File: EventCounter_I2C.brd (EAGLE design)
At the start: 38.7 x 20.8 mm, 32 parts, among them J1 CONN_42.54_SCREW, J2 CONN_32.54_SCREW, Q3 DMG3404, U1 TLV3691DCK, U11 SN74AUP3G34DCU, U12 TXS0102DQM, U2 TPS7A0533DBV, U7 ATTINY441/841VQFN, U8 SN74AUP1G34SC70

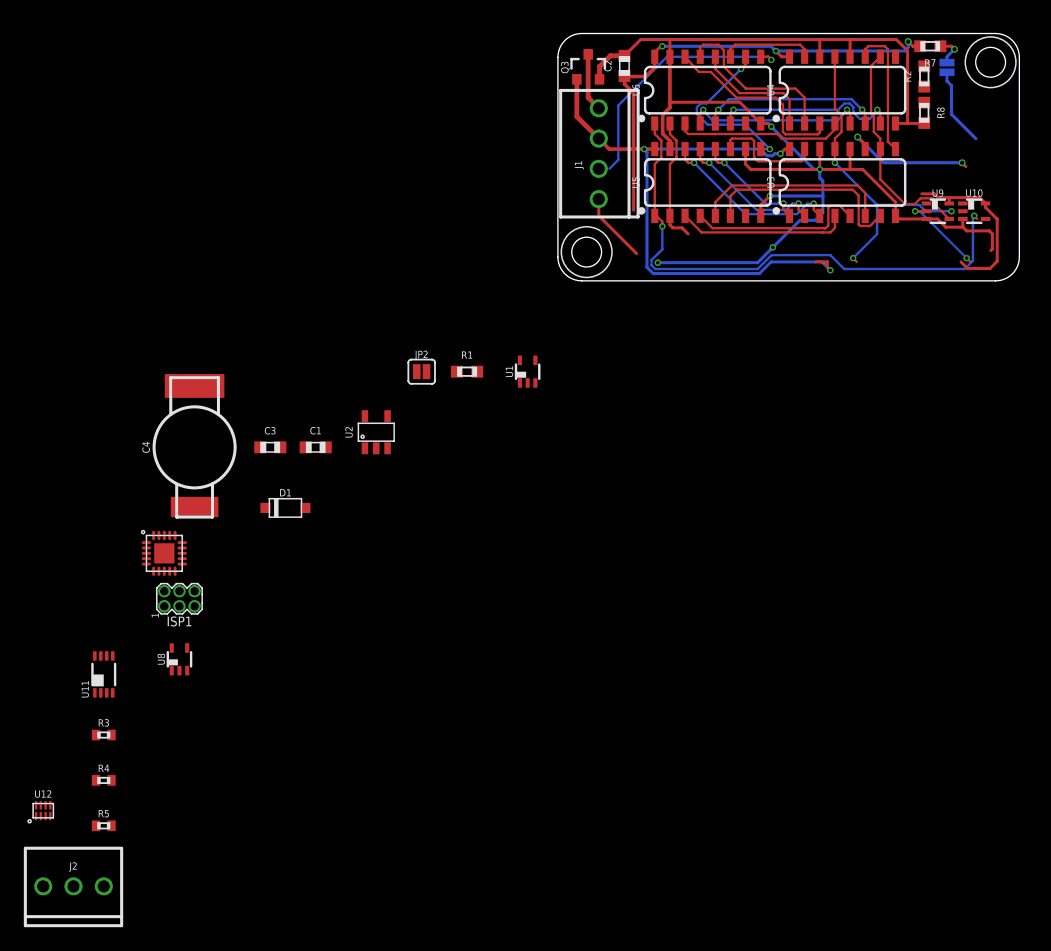
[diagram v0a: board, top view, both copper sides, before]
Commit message: Initial layout for I2C variant
First cut layout for I2C variant, passes DRC, still needs verification
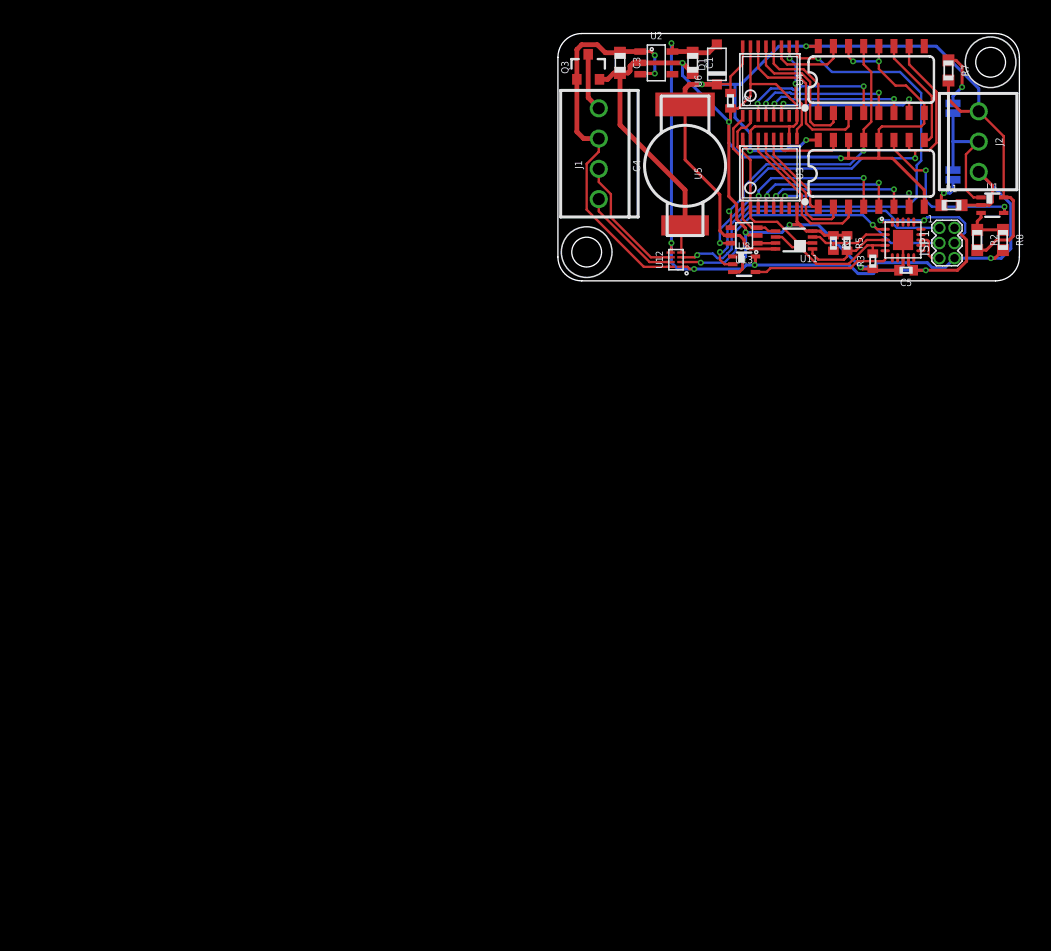
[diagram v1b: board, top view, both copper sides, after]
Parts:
- removed U10, U9: (no value), bschulz:DCK_R-PDSO-G5
- added C5: (no value), bschulz_passives:C0402
- added U13: (no value), bschulz:DCK_R-PDSO-G6
- C2: device bschulz_passives:C0603 -> bschulz_passives:C0402
- U5, U6: device bschulz:SO16 -> bschulz:TSSOP16
- moved J2 98.3 mm to (35.3, 11.7), turned to 270 degrees
- moved R5 79.2 mm to (24.3, 3.17), turned to 270 degrees
- moved R4 76.0 mm to (23.1, 3.17), turned to 270 degrees
- moved R3 75.8 mm to (26.4, 1.65), turned to 90 degrees
- moved ISP1 71.0 mm to (32.6, 3.17), turned to 270 degrees
- moved U12 70.4 mm to (9.91, 1.78), turned to 90 degrees
- moved U11 68.4 mm to (19.8, 3.43), turned to 90 degrees
- moved U7 67.3 mm to (29.0, 3.43)
- moved U8 57.8 mm to (15.6, 1.40), turned to 270 degrees
- moved D1 51.9 mm to (13.3, 18.2), turned to 90 degrees
- moved JP2 47.5 mm to (33.1, 8.89), flipped to the bottom, turned to 270 degrees
- moved C4 47.4 mm to (10.7, 9.65)
- moved C1 45.2 mm to (11.3, 18.3), turned to 270 degrees
- moved C3 43.6 mm to (5.21, 18.3), turned to 270 degrees
- moved R1 43.0 mm to (33.0, 6.35)
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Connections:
- removed net VCC: C2.1, C3.1, J1.3, Q3.1, R2.2, R7.2, U10.5, U12.8, U2.1, U2.3, U3.16, U4.16, U5.16, U6.16, U9.5
- new net VIN+: C3.1, J1.3, Q3.1, U12.8, U2.1, U2.3
- net !LOAD: now also U13.4; no longer U10.4
- net !RST: now also U13.6; no longer U9.4
- net 3V3: now also C5.1
- net CLK: now also U11.2; no longer U11.7
- net CLK_ISO: now also U11.6, U7.4; no longer U11.1
- net DATA_ISO: now also U7.5
- net GND: now also C5.2, U13.2; no longer U10.3, U9.3
- net LOAD: now also U11.5, U13.3; no longer U10.2, U11.2
- net LOAD_ISO: now also U11.3, U7.2; no longer U11.6
- net RST: now also U11.7, U13.1; no longer U11.5, U9.2
- net RST_ISO: now also U11.1, U7.3; no longer U11.3
- net V_CAP: now also C2.1, R2.2, R7.2, U13.5, U3.16, U4.16, U5.16, U6.16
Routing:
- net VCC: track 107.4 -> 0.00 mm, vias 6 -> 0
- net V_CAP: track 0.00 -> 89.4 mm, vias 0 -> 4
- net 3V3: track 0.00 -> 57.2 mm, vias 0 -> 5
- net GND: track 120.9 -> 161.0 mm, vias 5 -> 10
- net VIN+: track 0.00 -> 34.3 mm, vias 0 -> 2
- net LOAD: track 45.7 -> 12.5 mm, vias 2 -> 0
- net SDA: track 0.00 -> 30.3 mm, vias 0 -> 2
- net SCL: track 0.00 -> 26.5 mm, vias 0 -> 2
- net DATA: track 21.3 -> 42.7 mm, vias 1 -> 2
- net !RST: track 18.7 -> 34.6 mm, vias 0 -> 2
- net DATA_ISO: track 0.00 -> 12.0 mm
- net CLK_ISO: track 0.00 -> 11.4 mm
- net SDA_HV: track 0.00 -> 10.9 mm
- net RST_ISO: track 0.00 -> 7.69 mm
- net LOAD_ISO: track 0.00 -> 7.24 mm
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
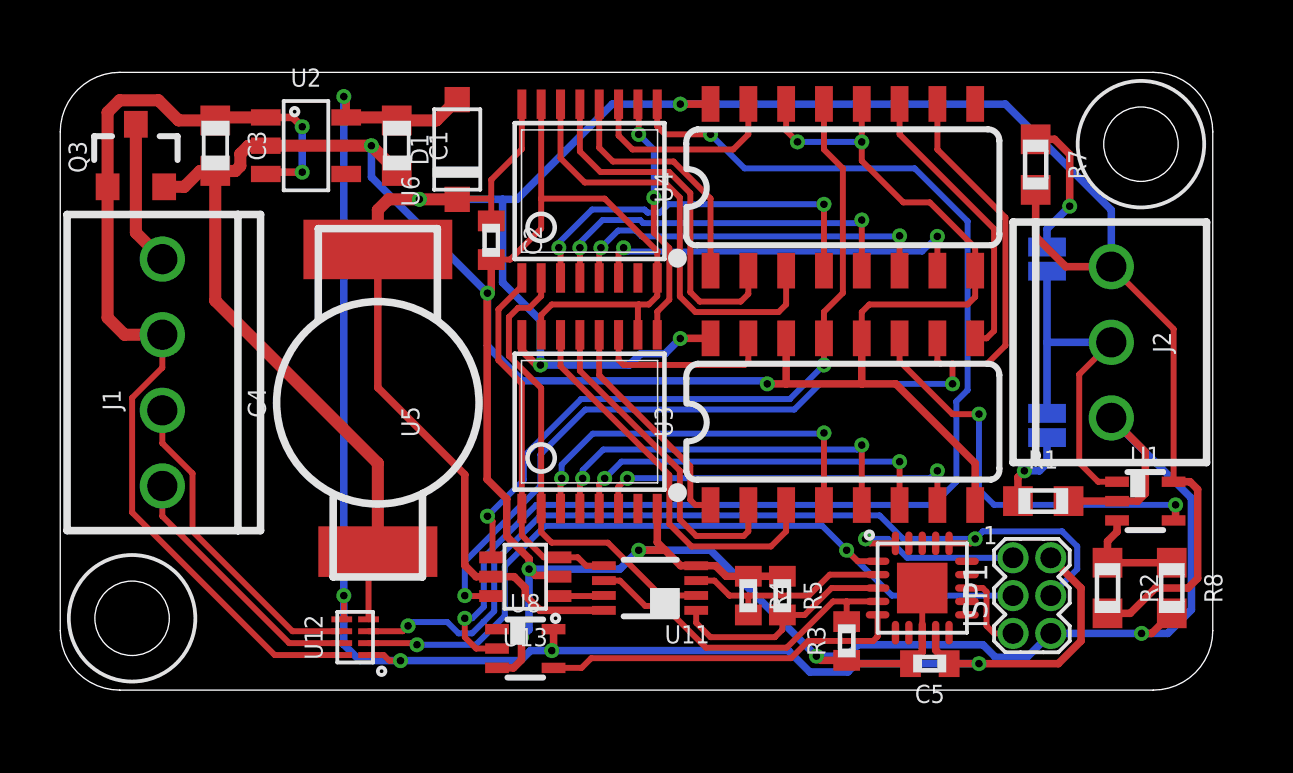
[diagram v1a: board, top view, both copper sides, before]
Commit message: Minor edits, sent to fab for v1.0 (I2C model)
Cleaned up layout, added pullup reset resistor, generated gerbers, sent v1.0 to fab
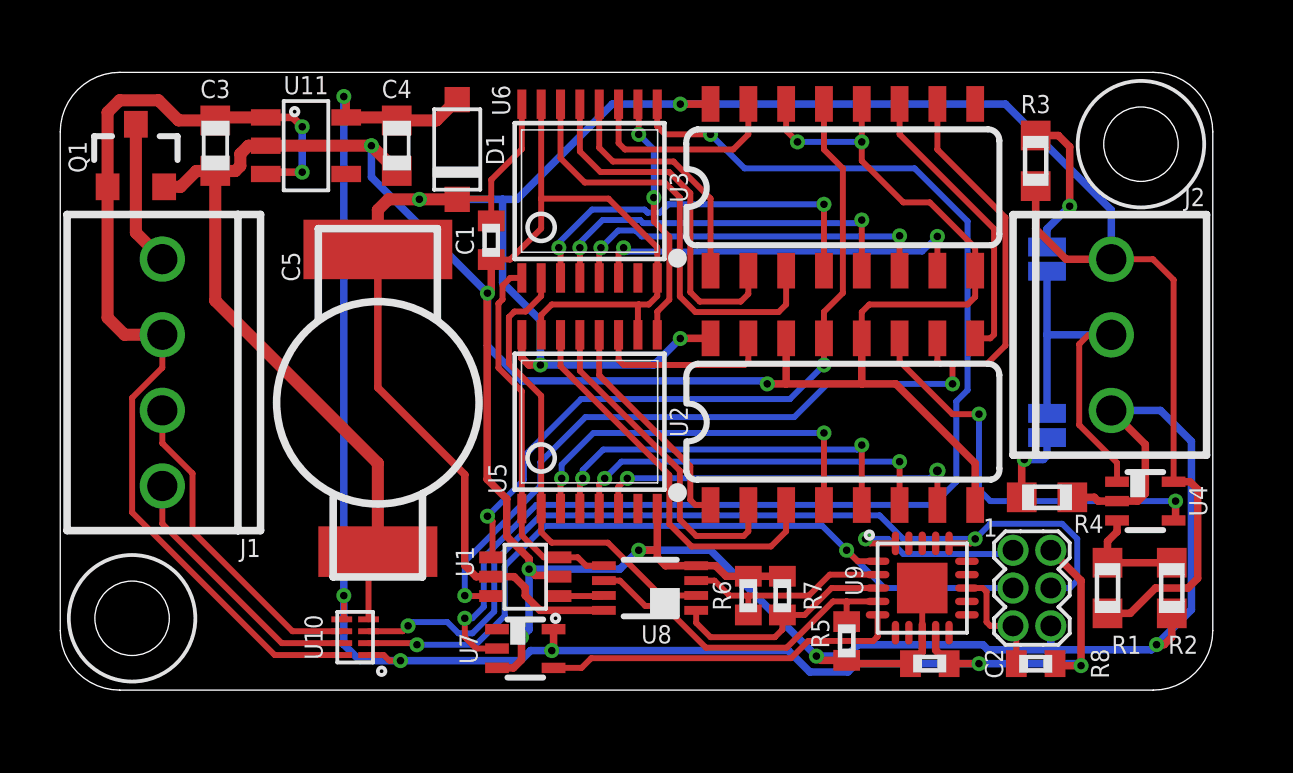
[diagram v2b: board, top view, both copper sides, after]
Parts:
- removed U13: (no value), bschulz:DCK_R-PDSO-G6
- added R6: 10k, bschulz_passives:R0402
- added U9: ATTINY441/841VQFN, bschulz:VQFN-20
- C1: value 1uF -> 0.1uF; device bschulz_passives:C0603 -> bschulz_passives:C0402
- C2: value 0.1uF -> (none)
- C4: value (none) -> 1uF; device bschulz_passives:HL -> bschulz_passives:C0603
- C5: device bschulz_passives:C0402 -> bschulz_passives:HL
- R3: value 10k -> 100k; device bschulz_passives:R0402 -> bschulz_passives:R0603
- R4: value 10k -> 10M; device bschulz_passives:R0402 -> bschulz_passives:R0603
- R7: value 100k -> 10k; device bschulz_passives:R0603 -> bschulz_passives:R0402
- R8: value 10M -> (none); device bschulz_passives:R0603 -> bschulz_passives:R0402
- U1: value TLV3691DCK -> (none); device bschulz:DCK_R-PDSO-G5 -> bschulz:DCK_R-PDSO-G6
- U11: value SN74AUP3G34DCU -> TPS7A0533DBV; device bschulz:DCU_(R-PDSO-G8) -> bschulz:SOT23-5
- U2: value TPS7A0533DBV -> (none); device bschulz:SOT23-5 -> bschulz:SO16
- U4: value (none) -> TLV3691DCK; device bschulz:SO16 -> bschulz:DCK_R-PDSO-G5
- U7: value ATTINY441/841VQFN -> SN74AUP1G34SC70; device bschulz:VQFN-20 -> bschulz:DCK_R-PDSO-G5
- U8: value SN74AUP1G34SC70 -> SN74AUP3G34DCU; device bschulz:DCK_R-PDSO-G5 -> bschulz:DCU_(R-PDSO-G8)
- moved U1 21.0 mm to (15.6, 3.81), turned to 90 degrees
- moved C5 20.5 mm to (10.7, 9.65), turned to 0 degrees
- moved C2 20.5 mm to (29.2, 0.89), turned to 180 degrees
- moved U2 20.3 mm to (26.3, 9.02), turned to 0 degrees
- moved U11 18.8 mm to (8.26, 18.3), turned to 270 degrees
- moved R3 17.3 mm to (32.8, 17.8), turned to 270 degrees
- moved R7 16.8 mm to (24.3, 3.17)
- moved U4 14.6 mm to (36.4, 6.35), turned to 270 degrees
- moved U7 13.5 mm to (15.6, 1.40), turned to 270 degrees
- moved R4 10.6 mm to (33.1, 6.48), turned to 0 degrees
- moved C4 8.66 mm to (11.3, 18.3), turned to 270 degrees
- moved U3 7.87 mm to (26.3, 16.9)
- moved R8 5.23 mm to (32.8, 0.89), turned to 0 degrees
- moved U8 4.66 mm to (19.8, 3.43), turned to 90 degrees
- moved C1 4.49 mm to (14.5, 15.1)
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- renumbered Q3 to Q1, U12 to U10
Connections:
- net !LOAD: now also U1.4, U2.13; no longer U13.4, U4.13
- net !RESET: now also R8.1, U9.13; no longer U7.13
- net !RST: now also U1.6, U2.10; no longer U13.6, U4.10
- net 3V3: now also C2.1, C4.1, R8.2, U11.5, U7.5, U9.9; no longer C1.1, C5.1, U2.5, U7.9, U8.5
- net CLK: now also U8.2; no longer U11.2
- net CLK_ISO: now also R5.2, U8.6, U9.4; no longer R3.2, U11.6, U7.4
- net DATA: now also U7.2; no longer U8.2
- net DATA_ISO: now also U7.4, U9.5; no longer U7.5, U8.4
- net GND: now also C4.2, C5.-, R2.2, R4.2, R6.1, R7.1, U11.2, U2.12, U2.14, U2.8, U4.2, U7.3, U8.4, U9.8, U9.EP; no longer C4.-, C5.2, R1.2, R3.1, R4.1, R8.2, U11.4, U13.2, U2.2, U4.12, U4.14, U4.8, U7.8, U7.EP, U8.3
- net LOAD: now also U1.3, U8.5; no longer U11.5, U13.3
- net LOAD_ISO: now also R6.2, U8.3, U9.2; no longer R4.2, U11.3, U7.2
- net MISO: now also U9.20; no longer U7.20
- net N$1: now also U3.15; no longer U4.15
- net N$10: now also U2.6; no longer U3.6
- net N$11: now also U2.5; no longer U3.5
- net N$12: now also U2.4; no longer U3.4
- net N$13: now also U2.3; no longer U3.3
- net N$14: now also U2.2; no longer U3.2
- net N$15: now also U2.1; no longer U3.1
- net N$16: now also U2.15; no longer U3.15
- net N$18: now also U2.9, U3.11; no longer U3.9, U4.11
- net N$19: now also R4.1; no longer R1.1
- net N$2: now also U3.1; no longer U4.1
- net N$20: now also R3.1; no longer R7.1
- net N$3: now also U3.2; no longer U4.2
- net N$4: now also U3.3; no longer U4.3
- net N$5: now also U3.4; no longer U4.4
- net N$6: now also U3.5; no longer U4.5
- net N$7: now also U3.6; no longer U4.6
- net N$8: now also U3.7; no longer U4.7
- net N$9: now also U2.7; no longer U3.7
- net PULSE: now also U4.1; no longer U1.1
- net PULSE_DIG: now also U2.11, U4.4; no longer U1.4, U3.11
- net RST: now also U1.1, U8.7; no longer U11.7, U13.1
- net RST_ISO: now also R7.2, U8.1, U9.3; no longer R5.2, U11.1, U7.3
- net SCL: now also U9.1; no longer U7.1
- net SDA: now also U9.16; no longer U7.16
- net VIN+: now also U11.1, U11.3; no longer U2.1, U2.3
- net VREF: now also R1.1, U4.3; no longer R8.1, U1.3
- net V_CAP: now also C1.1, C5.+, R1.2, R3.2, U2.16, U4.5, U8.8; no longer C2.1, C4.+, R2.2, R7.2, U11.8, U13.5, U4.16
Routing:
- net GND: track 161.0 -> 163.2 mm
- net 3V3: track 57.2 -> 58.9 mm, vias 5 -> 6
- net !RESET: track 2.85 -> 3.99 mm
- net V_CAP: track 89.4 -> 90.3 mm
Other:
- board text added: "J1"
- board text added: "Project Tally v1.0 -------------- Developed by Northern Widget and University of Minnesota"
- board text added: "Pulldown"
- board text added: "Pullup"
- board text added: "SCL"
- board text added: "SDA"
- board text added: "Vin+"
- board text added: "Vin-"
- board text removed: "Clk"
- board text removed: "Data"
- board text removed: "Project Tally v0.1 -------------- Developed by Northern Widget and University of Minnesota"

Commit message: Updated values/digikey info
Updated the part
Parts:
- C2: value (none) -> 0.1uF
- C5: value (none) -> 220mF
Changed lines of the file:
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@@
 <attribute name="VALUE" x="14.605" y="18.161" size="0.6096" layer="27" font="vector" ratio="15" rot="R90" align="center"/>
 </element>
-<element name="C5" library="bschulz_passives" package="HL" value="" x="10.668" y="9.652" smashed="yes">
+<element name="C5" library="bschulz_passives" package="HL" value="220mF" x="10.668" y="9.652" smashed="yes">
 <attribute name="NAME" x="7.747" y="14.224" size="0.6096" layer="25" font="vector" ratio="15" rot="R270" align="center"/>
 <attribute name="VALUE" x="14.605" y="9.652" size="0.6096" layer="27" font="vector" ratio="15" rot="R270" align="center"/>
@@
 <attribute name="VALUE" x="33.274" y="11.934" size="0.6096" layer="27" font="vector" ratio="20" rot="R270" align="bottom-center"/>
 </element>
-<element name="C2" library="bschulz_passives" package="C0402" value="" x="29.21" y="0.889" smashed="yes" rot="R180">
+<element name="C2" library="bschulz_passives" package="C0402" value="0.1uF" x="29.21" y="0.889" smashed="yes" rot="R180">
 <attribute name="DIGIKEY" value="490-4759-1-ND" x="29.21" y="0.889" size="1.778" layer="27" rot="R180" display="off"/>
 <attribute name="MF" value="Murata" x="29.21" y="0.889" size="1.778" layer="27" rot="R180" display="off"/>

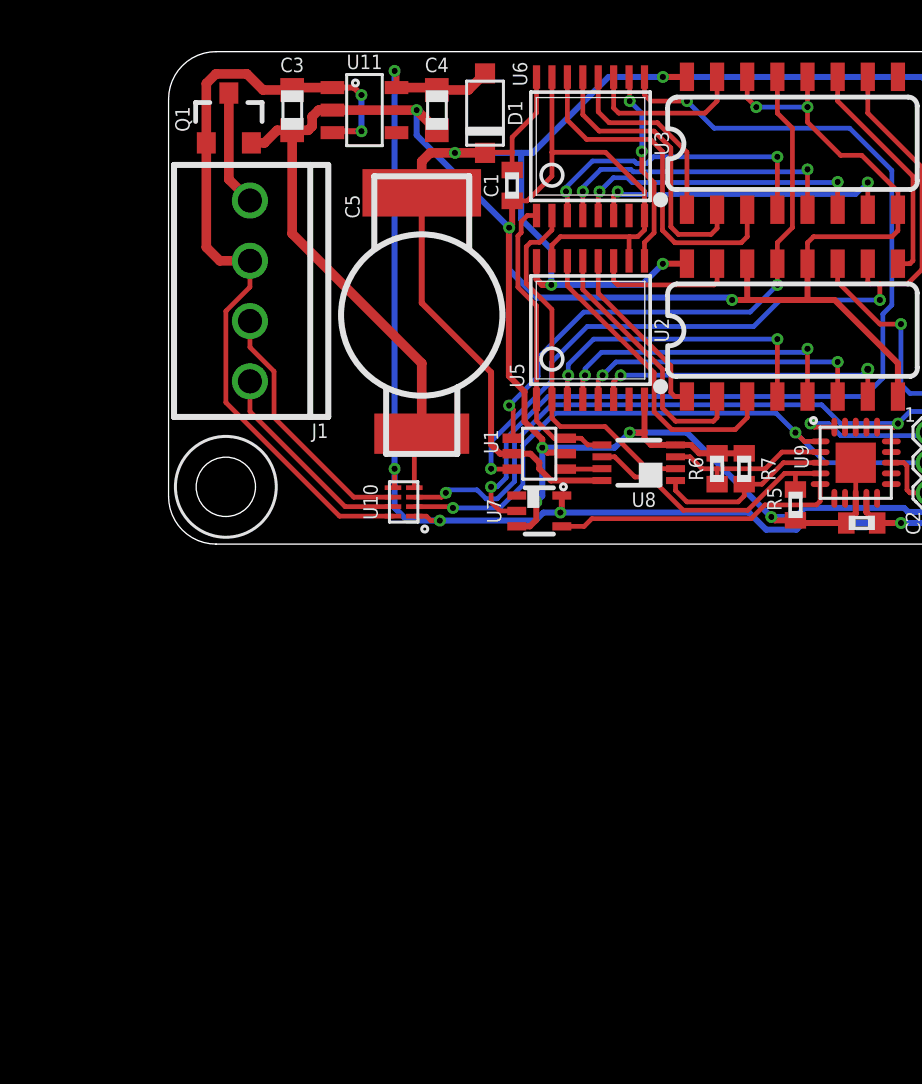
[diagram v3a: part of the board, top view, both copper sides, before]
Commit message: Updated firmware, minor design update
Improved firmware capabilities, added minor design updates to schematic, routing and feature decision still required
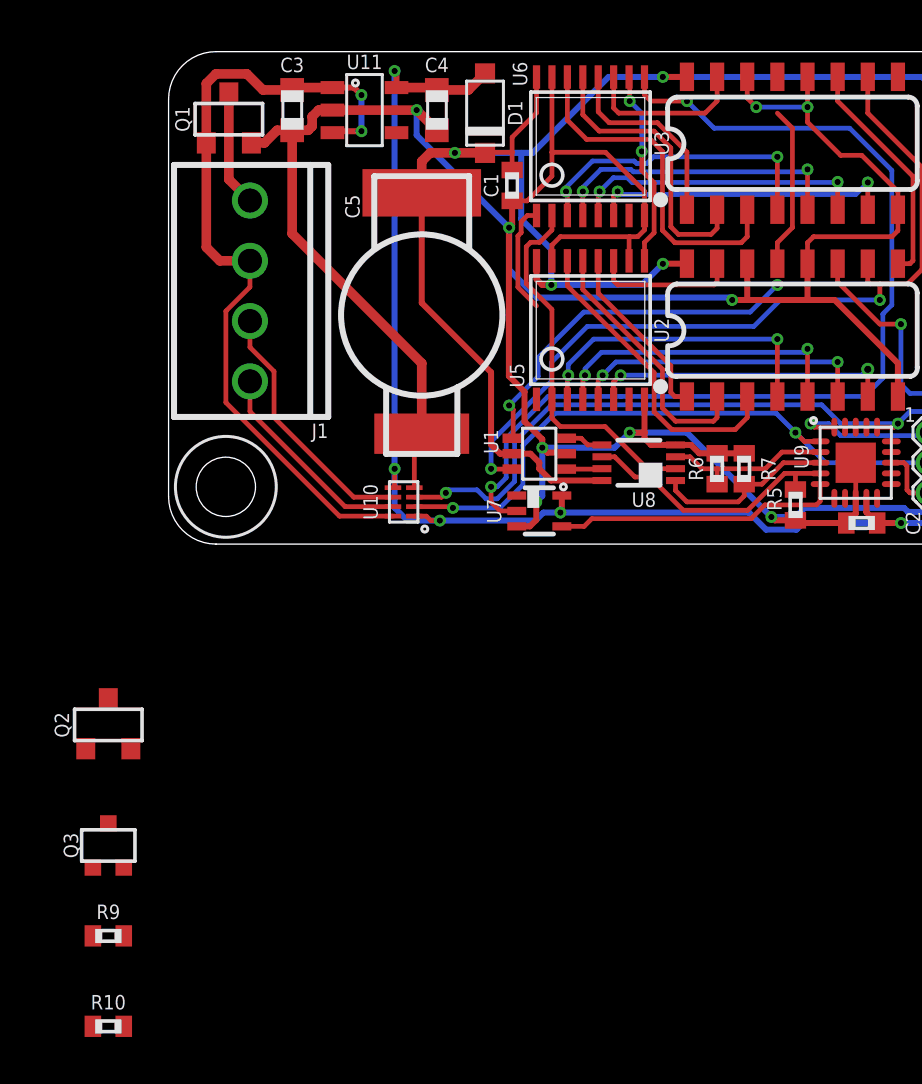
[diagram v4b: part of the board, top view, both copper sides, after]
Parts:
- added Q2: FDN360P, bschulz:SOT23-3
- added Q3: 2N7002, bschulz:SOT323
- added R10, R9: (no value), bschulz_passives:R0402
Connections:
- new net N$21: Q2.1, Q3.3, R9.1
- new net V_CAP_READ: Q2.3, U9.15
- net !LOAD: now also U5.1, U6.1; no longer U2.13, U3.13
- net GND: now also Q3.2, R10.1
- net LOAD: now also U2.13, U3.13; no longer U5.1, U6.1
- net VIN+: now also Q3.1, R10.2
- net V_CAP: now also Q2.2, R9.2
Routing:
- net !LOAD: track 24.6 -> 20.0 mm
- net LOAD: track 12.7 -> 8.53 mm
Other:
- board text added: "Project Tally v1.1 -------------- Developed by Northern Widget and University of Minnesota"
- board text removed: "Project Tally v1.0 -------------- Developed by Northern Widget and University of Minnesota"
